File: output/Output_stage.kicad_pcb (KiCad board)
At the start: 2 copper layers, 64.8 x 27.9 mm, 14 parts, among them J1 Conn_01x03_Socket, J2 Control/LED, J3 Control/LED, Q1 BTA41, U1 MOC3041M

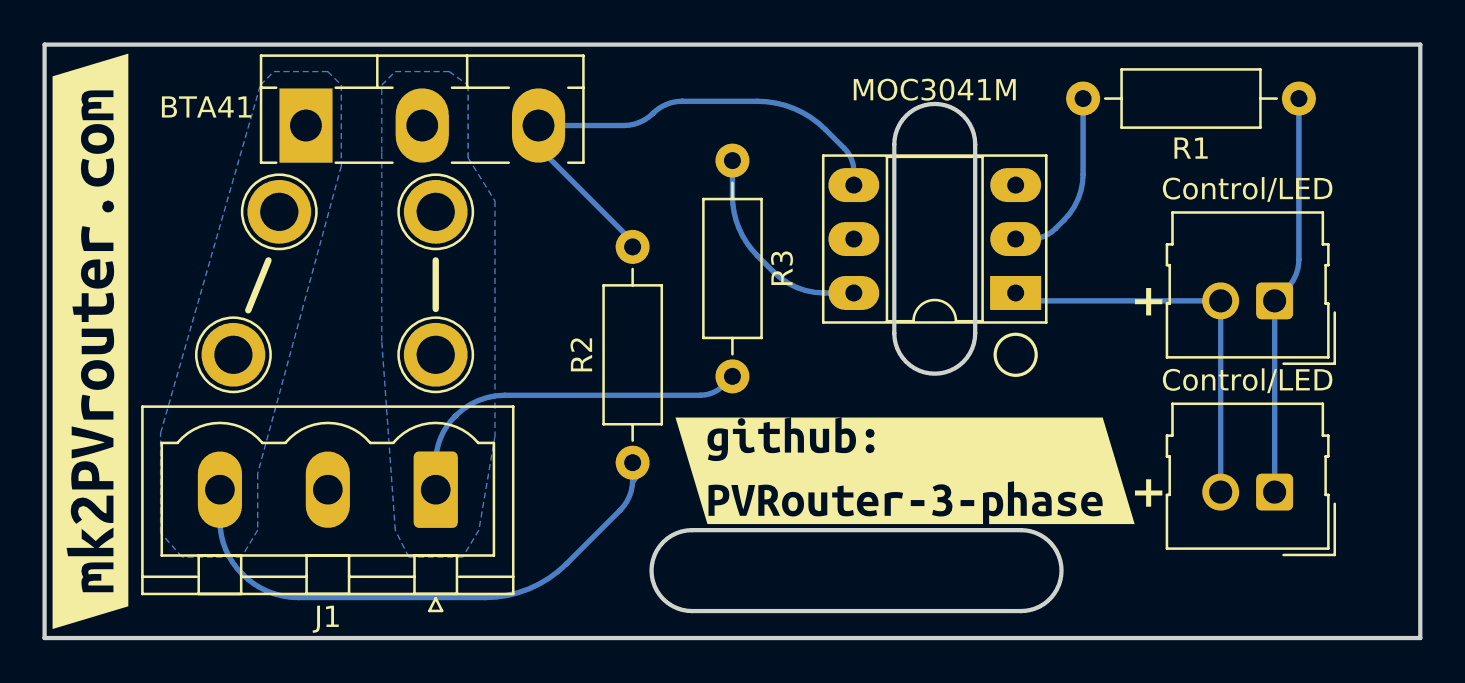
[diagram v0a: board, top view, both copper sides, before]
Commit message: Update some symbols/footprints
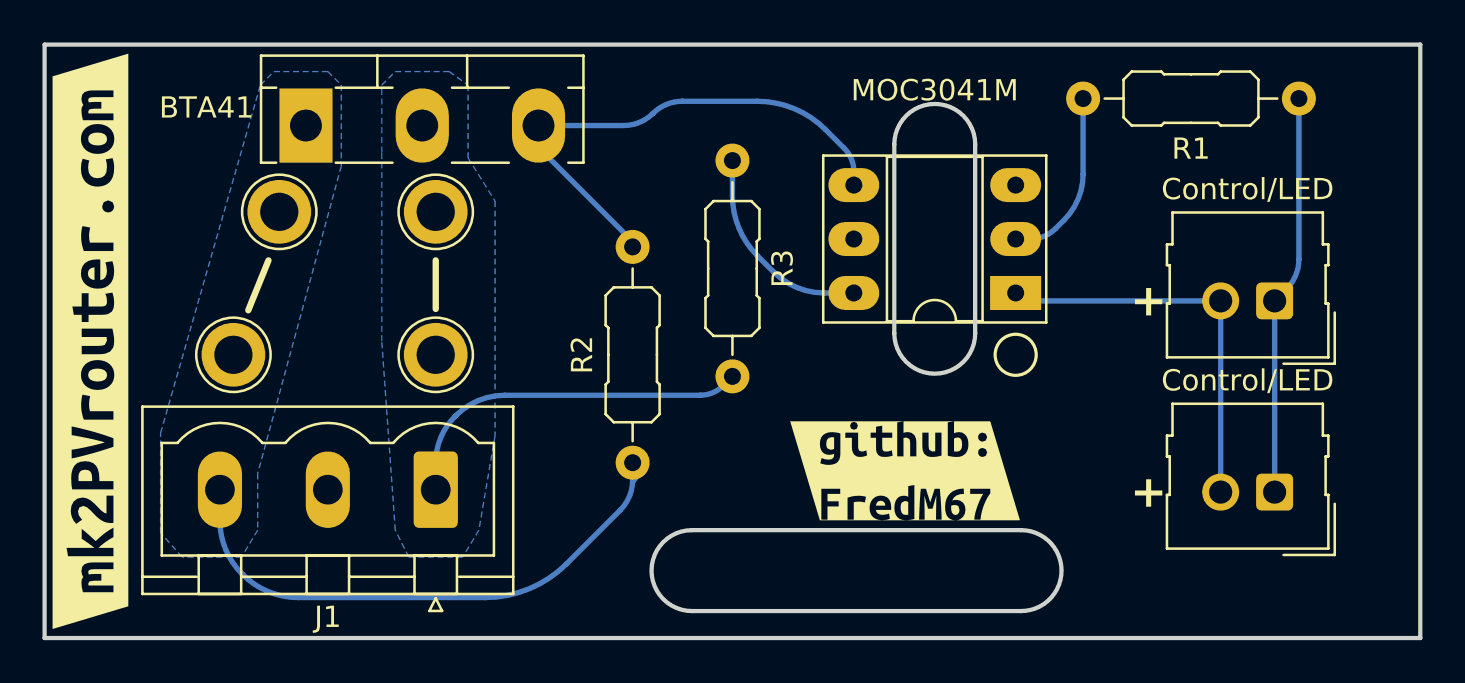
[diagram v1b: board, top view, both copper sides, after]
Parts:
- removed kibuzzard-6431D738: G***, kibuzzard-6431D738
- added kibuzzard-64A88973: G***, kibuzzard-64A88973, F.Cu at (78.0, 48.0)
- R1, R2, R3: footprint Resistor_THT:R_Axial_DIN0207_L6.3mm_D2.5mm_P10.16mm_Horizontal -> PCM_Resistor_THT_AKL:R_Axial_DIN0207_L6.3mm_D2.5mm_P10.16mm_Horizontal

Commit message: Update output
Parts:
- removed kibuzzard-64A88973: G***, kibuzzard-64A88973
- added REF**: Symbol_HighVoltage_Type2_CopperTop_VerySmall, Symbol:Symbol_HighVoltage_Type2_CopperTop_VerySmall, F.Cu at (72.4, 47.2)
- added REF**: Symbol_HighVoltage_Type2_CopperTop_VerySmall, Symbol:Symbol_HighVoltage_Type2_CopperTop_VerySmall, B.Cu at (72.4, 47.2)
- added kibuzzard-64EB09A8: G***, kibuzzard-64EB09A8, F.Cu at (100.8, 41.9)

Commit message: Some updates
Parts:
- removed the REF** at (72.4, 47.2) (x2)
- removed kibuzzard-64EB09A8: G***, kibuzzard-64EB09A8
- added REF**: Symbol_HighVoltage_Type2_Silk_VerySmall, Library:Symbol_HighVoltage_Type2_Silk_VerySmall, F.Cu at (72.2, 47.2)
- added REF**: Symbol_HighVoltage_Type2_Silk_VerySmall, Library:Symbol_HighVoltage_Type2_Silk_VerySmall, B.Cu at (72.2, 47.2)
- added kibuzzard-64EB64A3: G***, kibuzzard-64EB64A3, F.Cu at (100.6, 41.9)

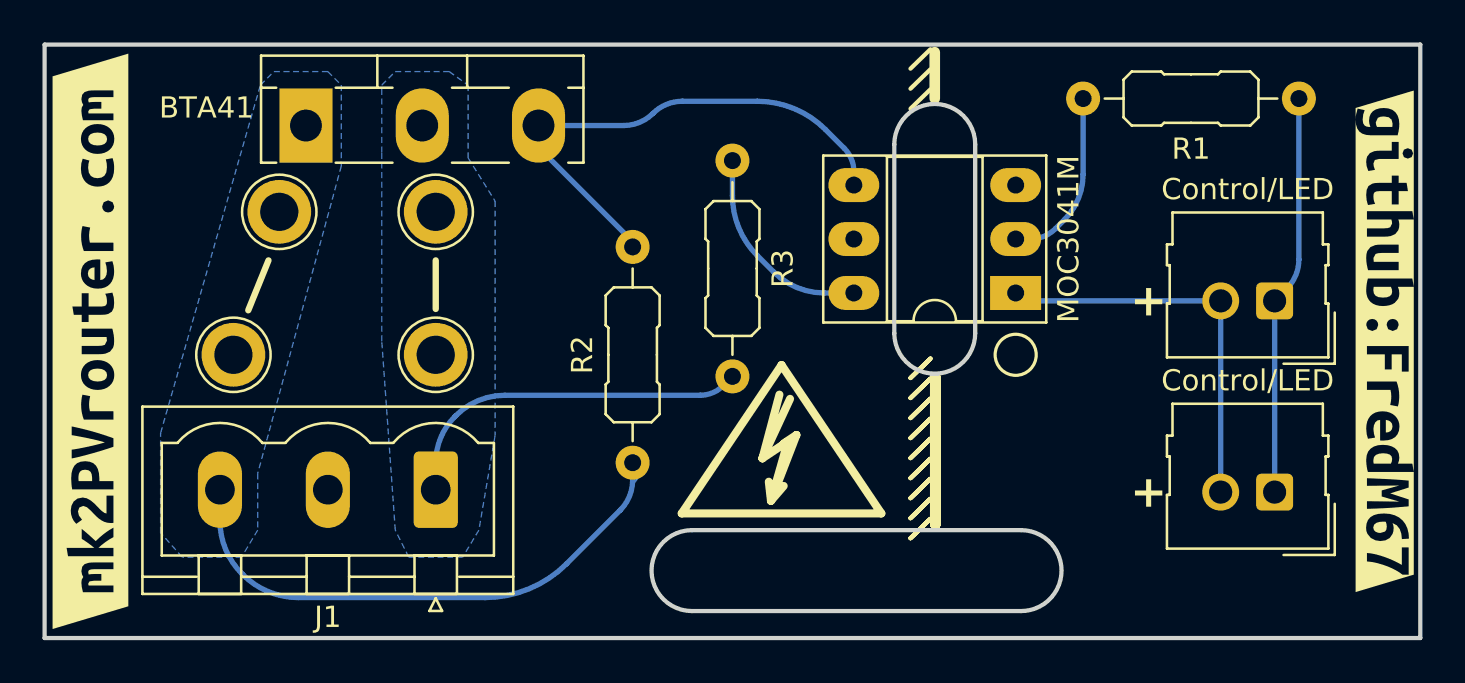
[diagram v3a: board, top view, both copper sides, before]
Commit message: Make LV track wider
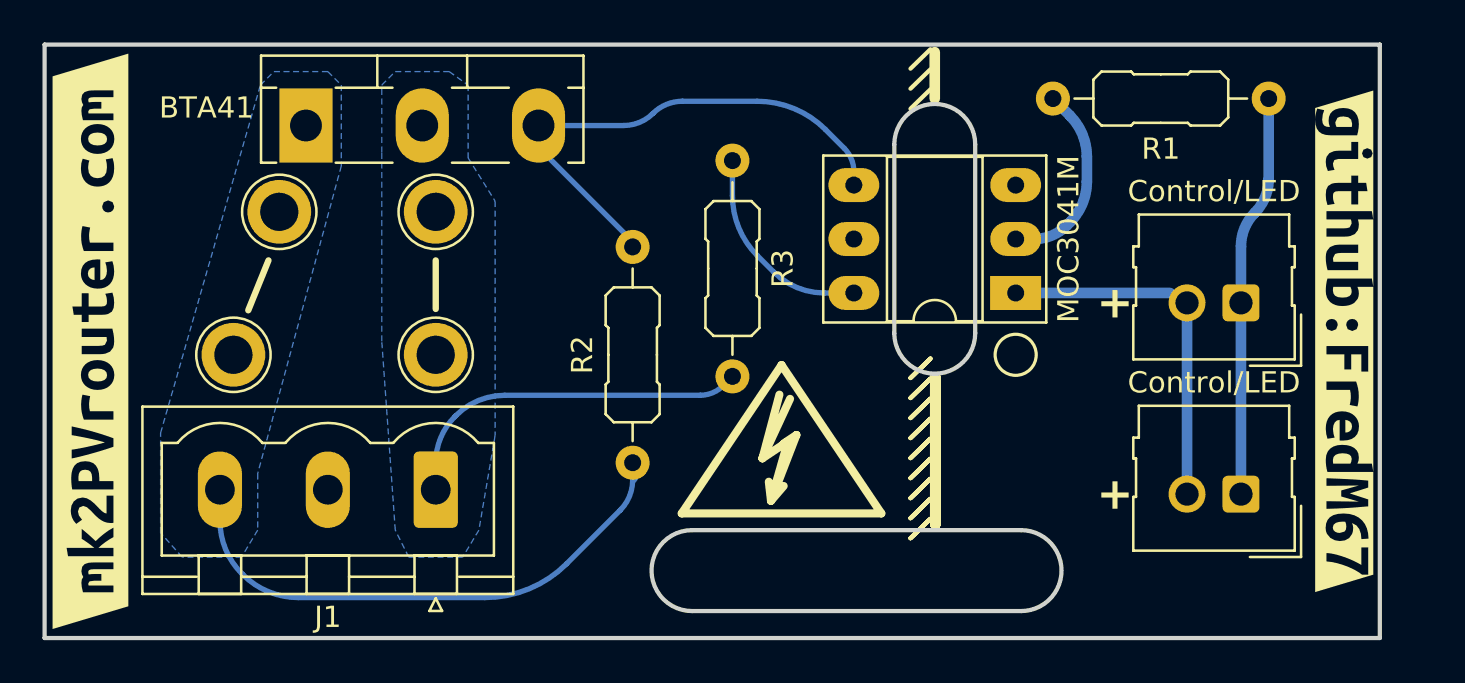
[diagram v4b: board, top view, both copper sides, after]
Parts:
- moved kibuzzard-64EB64A3 1.91 mm to (98.7, 41.9)
- moved J2 1.59 mm to (93.8, 40.1)
- moved J3 1.59 mm to (93.8, 49.1)
- moved R1 1.42 mm to (95.1, 30.5)
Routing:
- net Net-(J2-Pin_1): track 18.8 -> 19.7 mm
- net Net-(R1-Pad2): track 8.51 -> 9.34 mm
- net Net-(J2-Pin_2): track 18.0 -> 18.6 mm
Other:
- board size 64.8 x 27.9 mm -> 62.9 x 27.9 mm

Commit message: Tiny tuning
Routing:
- net LINE: track 17.3 -> 15.7 mm
- net Net-(J2-Pin_1): track 19.7 -> 19.0 mm
